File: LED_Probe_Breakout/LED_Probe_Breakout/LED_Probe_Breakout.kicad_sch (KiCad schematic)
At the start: 21 parts, among them J1 Conn_01x40, J10 Conn_Coaxial, J11 Conn_Coaxial, J12 Conn_Coaxial, J13 Conn_Coaxial, J14 Conn_Coaxial, J15 Conn_Coaxial, J16 Conn_Coaxial, J17 Conn_Coaxial, J2 Conn_Coaxial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

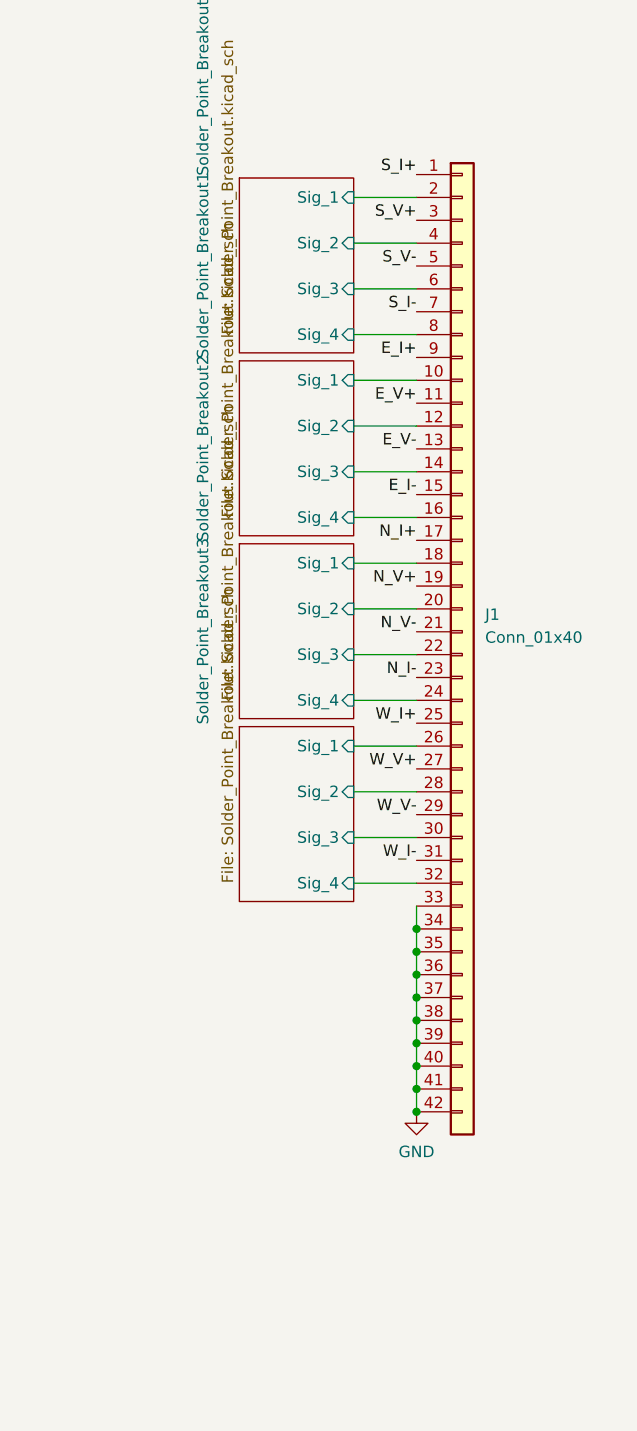
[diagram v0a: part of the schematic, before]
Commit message: update to 2x 20P
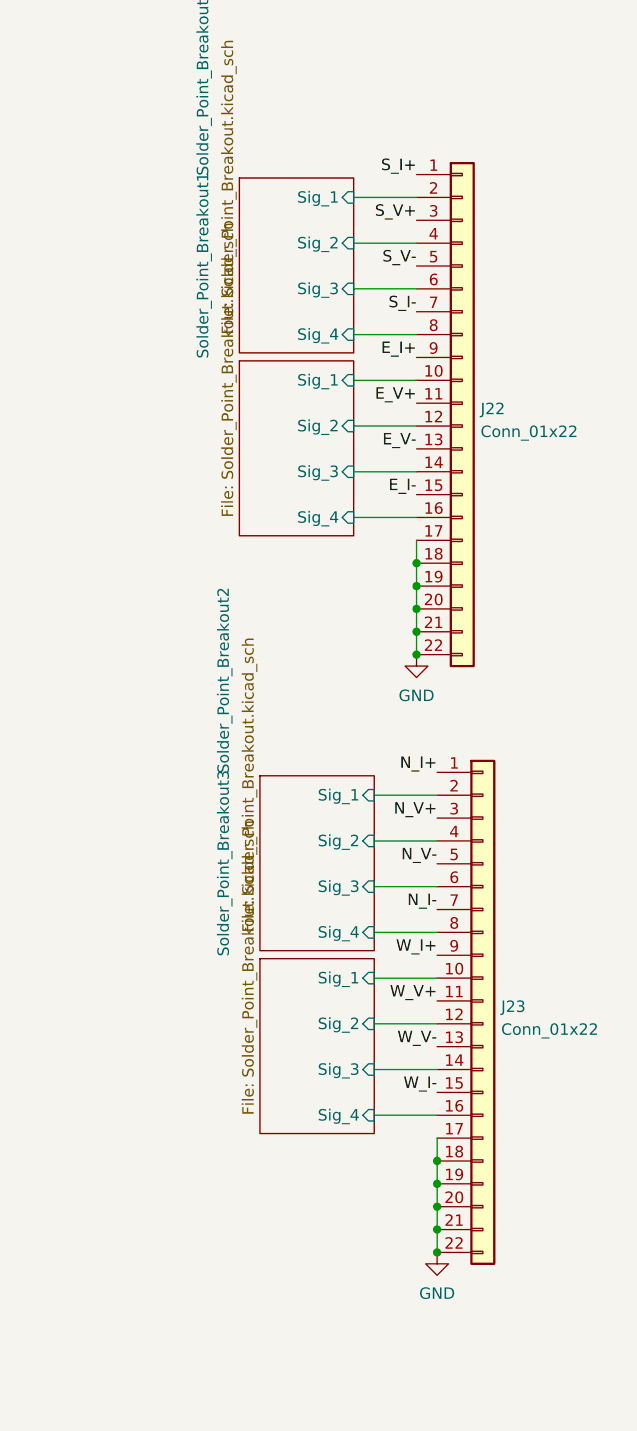
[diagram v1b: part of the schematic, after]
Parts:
- removed J1: Conn_01x40, 0_Breakout_footprint_lib:FPC-SMD_P0.50-40P_FGS-XJ-H2.0, symbol Connector_Generic:Conn_01x40
- added J22, J23: Conn_01x22, 0_Breakout_footprint_lib:FPC-SMD_20P-P0.50_XUNPU_FPC-05F-20PH20, symbol Connector_Generic:Conn_01x22
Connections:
- net E_I+: now also J22.9 (Pin_9)
- net E_I-: now also J22.15 (Pin_15)
- net E_V+: now also J22.11 (Pin_11)
- net E_V-: now also J22.13 (Pin_13)
- net GND: now also J22.17 (Pin_17), J22.18 (Pin_18), J22.19 (Pin_19), J22.20 (Pin_20), J22.21 (Pin_21), J22.22 (Pin_22), J23.17 (Pin_17), J23.18 (Pin_18), J23.19 (Pin_19), J23.20 (Pin_20), J23.21 (Pin_21), J23.22 (Pin_22)
- net N_I+: now also J23.1 (Pin_1)
- net N_I-: now also J23.7 (Pin_7)
- net N_V+: now also J23.3 (Pin_3)
- net N_V-: now also J23.5 (Pin_5)
- net S_I+: now also J22.1 (Pin_1)
- net S_I-: now also J22.7 (Pin_7)
- net S_V+: now also J22.3 (Pin_3)
- net S_V-: now also J22.5 (Pin_5)
- net Solder_Point_Breakout/Sig_1: now also J22.2 (Pin_2)
- net Solder_Point_Breakout/Sig_2: now also J22.4 (Pin_4)
- net Solder_Point_Breakout/Sig_3: now also J22.6 (Pin_6)
- net Solder_Point_Breakout/Sig_4: now also J22.8 (Pin_8)
- net Solder_Point_Breakout1/Sig_1: now also J22.10 (Pin_10)
- net Solder_Point_Breakout1/Sig_2: now also J22.12 (Pin_12)
- net Solder_Point_Breakout1/Sig_3: now also J22.14 (Pin_14)
- net Solder_Point_Breakout1/Sig_4: now also J22.16 (Pin_16)
- net Solder_Point_Breakout2/Sig_1: now also J23.2 (Pin_2)
- net Solder_Point_Breakout2/Sig_2: now also J23.4 (Pin_4)
- net Solder_Point_Breakout2/Sig_3: now also J23.6 (Pin_6)
- net Solder_Point_Breakout2/Sig_4: now also J23.8 (Pin_8)
- net Solder_Point_Breakout3/Sig_1: now also J23.10 (Pin_10)
- net Solder_Point_Breakout3/Sig_2: now also J23.12 (Pin_12)
- net Solder_Point_Breakout3/Sig_3: now also J23.14 (Pin_14)
- net Solder_Point_Breakout3/Sig_4: now also J23.16 (Pin_16)
- net W_I+: now also J23.9 (Pin_9)
- net W_I-: now also J23.15 (Pin_15)
- net W_V+: now also J23.11 (Pin_11)
- net W_V-: now also J23.13 (Pin_13)
